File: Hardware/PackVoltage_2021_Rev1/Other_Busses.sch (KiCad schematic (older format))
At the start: 50 parts, among them Q10 Q_NMOS_DGS, Q6 Q_NMOS_DGS, Q7 Q_NMOS_DGS, Q8 Q_NMOS_DGS, Q9 Q_NMOS_DGS, U14 LT1910, U15 LT1910, U16 LT1910, U17 INA281, U18 INA281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

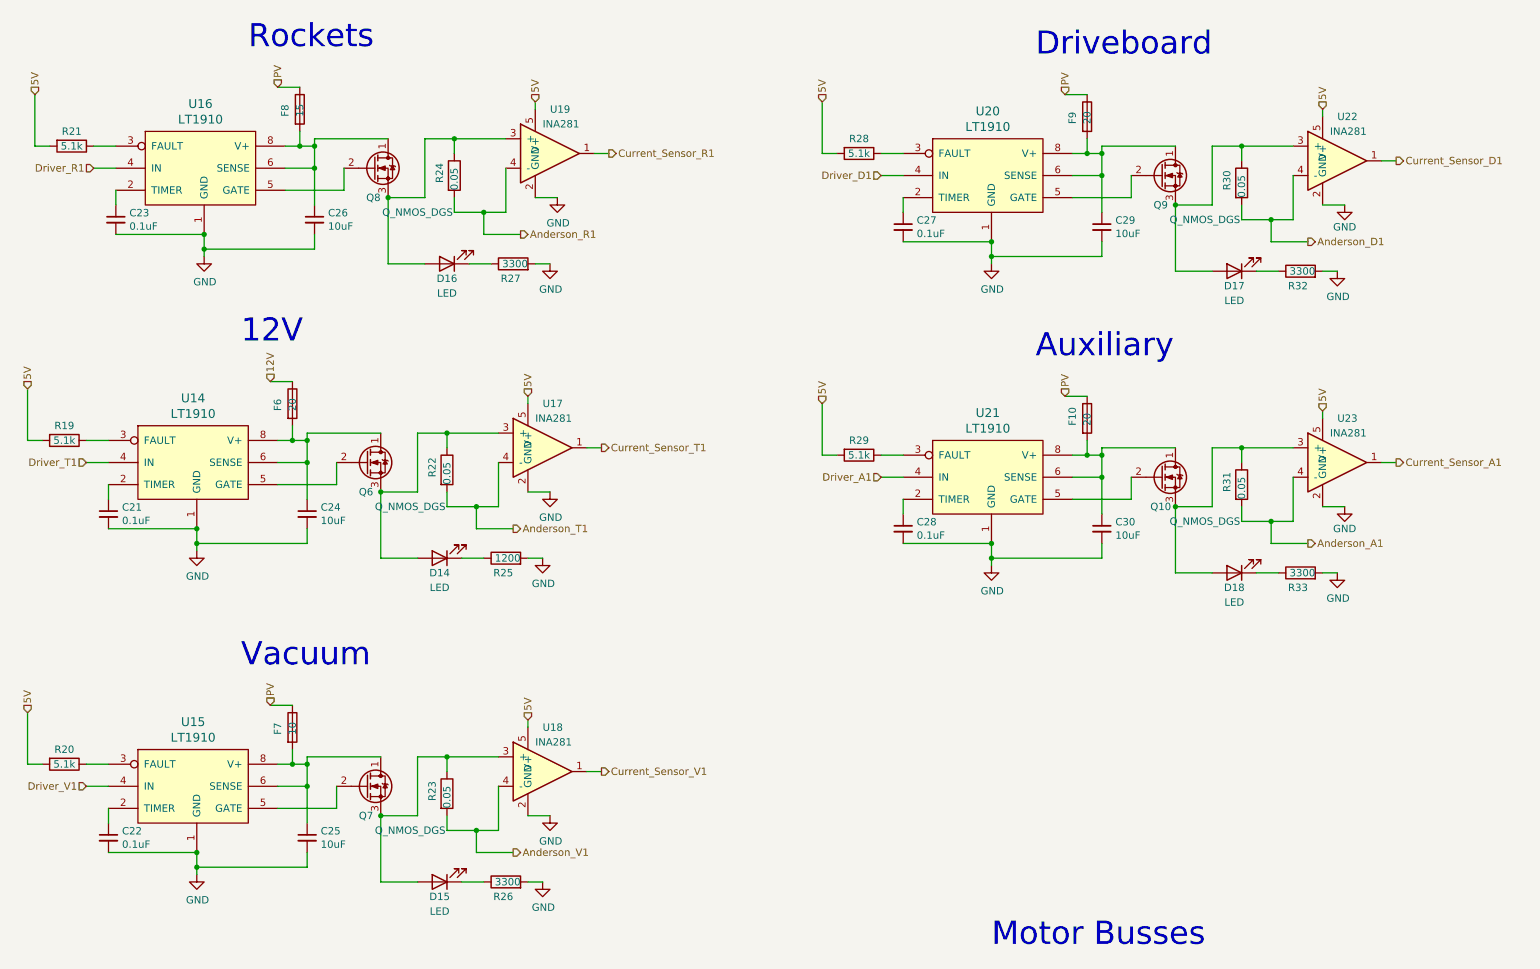
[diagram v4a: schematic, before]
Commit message: Finished Busses, Fixed Vias in Pads, Connected Okis & Buck
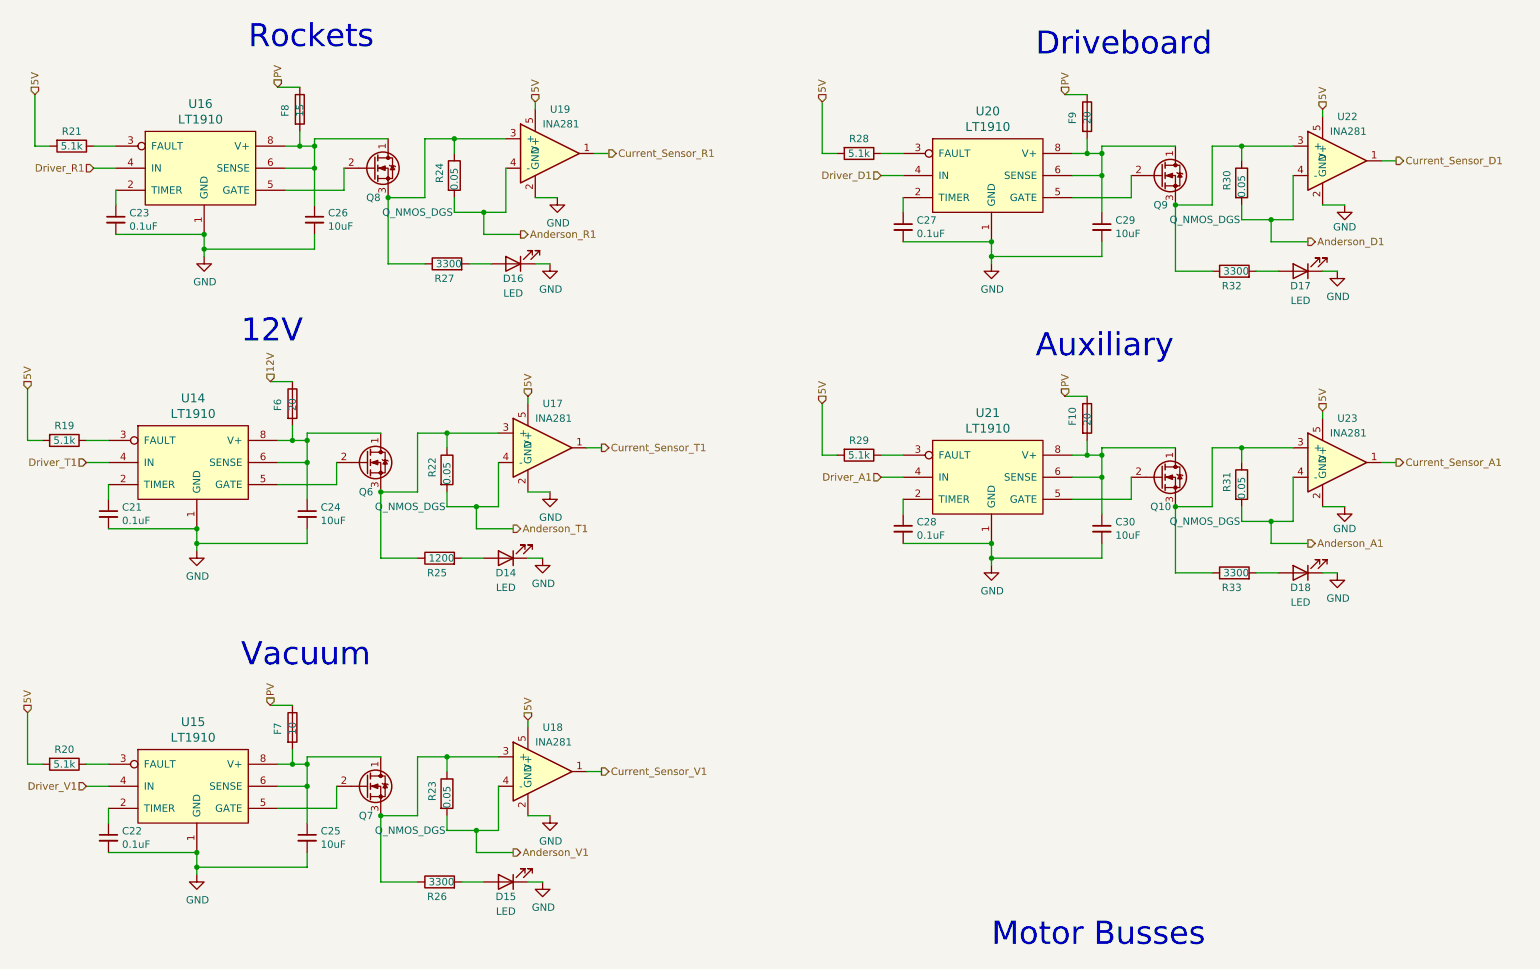
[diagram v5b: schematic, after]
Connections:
- net GND: now also D14.1 (K), D15.1 (K), D16.1 (K), D17.1 (K), D18.1 (K); no longer R25.2, R26.2, R27.2, R32.2, R33.2
- net at Q8.3 (S), R24.1, U19.3 (+): now also R27.1; no longer D16.2 (A)
- net at Q7.3 (S), R23.1, U18.3 (+): now also R26.1; no longer D15.2 (A)
- net at Q9.3 (S), R30.1, U22.3 (+): now also R32.1; no longer D17.2 (A)
- net at Q10.3 (S), R31.1, U23.3 (+): now also R33.1; no longer D18.2 (A)
- net at Q6.3 (S), R22.1, U17.3 (+): now also R25.1; no longer D14.2 (A)
- new net: D16.2 (A), R27.2
- new net: D15.2 (A), R26.2
- new net: D17.2 (A), R32.2
- new net: D18.2 (A), R33.2
- new net: D14.2 (A), R25.2
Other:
- moved on the sheet: D14, D15, D16, D17, D18, R25, R26, R27, R32, R33
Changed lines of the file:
@@
 L Device:LED D?
 U 1 1 5F846899
-P 3500 2300
+P 3950 2300
 AR Path="/5F7A6A8B/5F846899" Ref="D?"  Part="1"
 AR Path="/5F8EFCC9/5F846899" Ref="D16"  Part="1"
-F 0 "D16" H 3500 2400 50  0000 C CNN
-F 1 "LED" H 3500 2500 50  0000 C CNN
-F 2 "LED_SMD:LED_0603_1608Metric_Pad1.05x0.95mm_HandSolder" H 3500 2300 50  0001 C CNN
+F 0 "D16" H 3950 2400 50  0000 C CNN
+F 1 "LED" H 3950 2500 50  0000 C CNN
+F 2 "LED_SMD:LED_0603_1608Metric_Pad1.05x0.95mm_HandSolder" H 3950 2300 50  0001 C CNN
+F 3 "~" H 3950 2300 50  0001 C CNN
+	1    3950 2300
+	-1   0    0    1
+$EndComp
+Wire Wire Line
+	3100 2300 3350 2300
+$Comp
+L Device:R R?
+U 1 1 5F9AF792
+P 3500 2300
+AR Path="/5F7A6A8B/5F9AF792" Ref="R?"  Part="1"
+AR Path="/5F8EFCC9/5F9AF792" Ref="R27"  Part="1"
+F 0 "R27" V 3400 2250 50  0000 L CNN
+F 1 "3300" V 3500 2200 50  0000 L CNN
+F 2 "Resistor_SMD:R_0603_1608Metric_Pad1.05x0.95mm_HandSolder" V 3430 2300 50  0001 C CNN
 F 3 "~" H 3500 2300 50  0001 C CNN
 	1    3500 2300
-	-1   0    0    1
-$EndComp
-Wire Wire Line
-	3100 2300 3350 2300
-$Comp
-L Device:R R?
-U 1 1 5F9AF792
-P 3950 2300
-AR Path="/5F7A6A8B/5F9AF792" Ref="R?"  Part="1"
-AR Path="/5F8EFCC9/5F9AF792" Ref="R27"  Part="1"
-F 0 "R27" V 3850 2250 50  0000 L CNN
-F 1 "3300" V 3950 2200 50  0000 L CNN
-F 2 "Resistor_SMD:R_0603_1608Metric_Pad1.05x0.95mm_HandSolder" V 3880 2300 50  0001 C CNN
-F 3 "~" H 3950 2300 50  0001 C CNN
-	1    3950 2300
 	0    -1   -1   0
 $EndComp
@@
 	1    0    0    -1
 $EndComp
-$Comp
-L Device:LED D?
-U 1 1 5F9AF79C
-P 3450 4300
-AR Path="/5F7A6A8B/5F9AF79C" Ref="D?"  Part="1"
-AR Path="/5F8EFCC9/5F9AF79C" Ref="D14"  Part="1"
-F 0 "D14" H 3450 4400 50  0000 C CNN
-F 1 "LED" H 3450 4500 50  0000 C CNN
-F 2 "LED_SMD:LED_0603_1608Metric_Pad1.05x0.95mm_HandSolder" H 3450 4300 50  0001 C CNN
-F 3 "~" H 3450 4300 50  0001 C CNN
-	1    3450 4300
-	-1   0    0    1
-$EndComp
 Wire Wire Line
 	3050 4300 3300 4300
@@
 L Device:LED D?
 U 1 1 5F8A5A26
-P 3450 6500
+P 3900 6500
 AR Path="/5F7A6A8B/5F8A5A26" Ref="D?"  Part="1"
 AR Path="/5F8EFCC9/5F8A5A26" Ref="D15"  Part="1"
-F 0 "D15" H 3450 6600 50  0000 C CNN
-F 1 "LED" H 3450 6700 50  0000 C CNN
-F 2 "LED_SMD:LED_0603_1608Metric_Pad1.05x0.95mm_HandSolder" H 3450 6500 50  0001 C CNN
-F 3 "~" H 3450 6500 50  0001 C CNN
-	1    3450 6500
+F 0 "D15" H 3900 6600 50  0000 C CNN
+F 1 "LED" H 3900 6700 50  0000 C CNN
+F 2 "LED_SMD:LED_0603_1608Metric_Pad1.05x0.95mm_HandSolder" H 3900 6500 50  0001 C CNN
+F 3 "~" H 3900 6500 50  0001 C CNN
+	1    3900 6500
 	-1   0    0    1
 $EndComp
@@
 L Device:LED D?
 U 1 1 5F8B2B79
-P 8850 2350
+P 9300 2350
 AR Path="/5F7A6A8B/5F8B2B79" Ref="D?"  Part="1"
 AR Path="/5F8EFCC9/5F8B2B79" Ref="D17"  Part="1"
-F 0 "D17" H 8850 2450 50  0000 C CNN
-F 1 "LED" H 8850 2550 50  0000 C CNN
-F 2 "LED_SMD:LED_0603_1608Metric_Pad1.05x0.95mm_HandSolder" H 8850 2350 50  0001 C CNN
+F 0 "D17" H 9300 2450 50  0000 C CNN
+F 1 "LED" H 9300 2550 50  0000 C CNN
+F 2 "LED_SMD:LED_0603_1608Metric_Pad1.05x0.95mm_HandSolder" H 9300 2350 50  0001 C CNN
+F 3 "~" H 9300 2350 50  0001 C CNN
+	1    9300 2350
+	-1   0    0    1
+$EndComp
+Wire Wire Line
+	8450 2350 8700 2350
+$Comp
+L Device:R R?
+U 1 1 5F9AF7B7
+P 8850 2350
+AR Path="/5F7A6A8B/5F9AF7B7" Ref="R?"  Part="1"
+AR Path="/5F8EFCC9/5F9AF7B7" Ref="R32"  Part="1"
+F 0 "R32" V 8750 2300 50  0000 L CNN
+F 1 "3300" V 8850 2250 50  0000 L CNN
+F 2 "Resistor_SMD:R_0603_1608Metric_Pad1.05x0.95mm_HandSolder" V 8780 2350 50  0001 C CNN
 F 3 "~" H 8850 2350 50  0001 C CNN
 	1    8850 2350
-	-1   0    0    1
-$EndComp
-Wire Wire Line
-	8450 2350 8700 2350
-$Comp
-L Device:R R?
-U 1 1 5F9AF7B7
-P 9300 2350
-AR Path="/5F7A6A8B/5F9AF7B7" Ref="R?"  Part="1"
-AR Path="/5F8EFCC9/5F9AF7B7" Ref="R32"  Part="1"
-F 0 "R32" V 9200 2300 50  0000 L CNN
-F 1 "3300" V 9300 2250 50  0000 L CNN
-F 2 "Resistor_SMD:R_0603_1608Metric_Pad1.05x0.95mm_HandSolder" V 9230 2350 50  0001 C CNN
-F 3 "~" H 9300 2350 50  0001 C CNN
-	1    9300 2350
 	0    -1   -1   0
 $EndComp
@@
 L Device:LED D?
 U 1 1 5F8E4236
-P 8850 4400
+P 9300 4400
 AR Path="/5F7A6A8B/5F8E4236" Ref="D?"  Part="1"
 AR Path="/5F8EFCC9/5F8E4236" Ref="D18"  Part="1"
-F 0 "D18" H 8850 4500 50  0000 C CNN
-F 1 "LED" H 8850 4600 50  0000 C CNN
-F 2 "LED_SMD:LED_0603_1608Metric_Pad1.05x0.95mm_HandSolder" H 8850 4400 50  0001 C CNN
+F 0 "D18" H 9300 4500 50  0000 C CNN
+F 1 "LED" H 9300 4600 50  0000 C CNN
+F 2 "LED_SMD:LED_0603_1608Metric_Pad1.05x0.95mm_HandSolder" H 9300 4400 50  0001 C CNN
+F 3 "~" H 9300 4400 50  0001 C CNN
+	1    9300 4400
+	-1   0    0    1
+$EndComp
+Wire Wire Line
+	8450 4400 8700 4400
+$Comp
+L Device:R R?
+U 1 1 5F8E423D
+P 8850 4400
+AR Path="/5F7A6A8B/5F8E423D" Ref="R?"  Part="1"
+AR Path="/5F8EFCC9/5F8E423D" Ref="R33"  Part="1"
+F 0 "R33" V 8750 4350 50  0000 L CNN
+F 1 "3300" V 8850 4300 50  0000 L CNN
+F 2 "Resistor_SMD:R_0603_1608Metric_Pad1.05x0.95mm_HandSolder" V 8780 4400 50  0001 C CNN
 F 3 "~" H 8850 4400 50  0001 C CNN
 	1    8850 4400
-	-1   0    0    1
-$EndComp
-Wire Wire Line
-	8450 4400 8700 4400
-$Comp
-L Device:R R?
-U 1 1 5F8E423D
-P 9300 4400
-AR Path="/5F7A6A8B/5F8E423D" Ref="R?"  Part="1"
-AR Path="/5F8EFCC9/5F8E423D" Ref="R33"  Part="1"
-F 0 "R33" V 9200 4350 50  0000 L CNN
-F 1 "3300" V 9300 4300 50  0000 L CNN
-F 2 "Resistor_SMD:R_0603_1608Metric_Pad1.05x0.95mm_HandSolder" V 9230 4400 50  0001 C CNN
-F 3 "~" H 9300 4400 50  0001 C CNN
-	1    9300 4400
 	0    -1   -1   0
 $EndComp
@@
 $Comp
 L Device:R R?
+U 1 1 5F9AF79D
+P 3450 4300
+AR Path="/5F7A6A8B/5F9AF79D" Ref="R?"  Part="1"
+AR Path="/5F8EFCC9/5F9AF79D" Ref="R25"  Part="1"
+F 0 "R25" V 3350 4250 50  0000 L CNN
+F 1 "1200" V 3450 4200 50  0000 L CNN
+F 2 "Resistor_SMD:R_0603_1608Metric_Pad1.05x0.95mm_HandSolder" V 3380 4300 50  0001 C CNN
+F 3 "~" H 3450 4300 50  0001 C CNN
+	1    3450 4300
+	0    -1   -1   0
+$EndComp
+$Comp
+L Device:LED D?
+U 1 1 5F9AF79C
+P 3900 4300
+AR Path="/5F7A6A8B/5F9AF79C" Ref="D?"  Part="1"
+AR Path="/5F8EFCC9/5F9AF79C" Ref="D14"  Part="1"
+F 0 "D14" H 3900 4400 50  0000 C CNN
+F 1 "LED" H 3900 4500 50  0000 C CNN
+F 2 "LED_SMD:LED_0603_1608Metric_Pad1.05x0.95mm_HandSolder" H 3900 4300 50  0001 C CNN
+F 3 "~" H 3900 4300 50  0001 C CNN
+	1    3900 4300
+	-1   0    0    1
+$EndComp
+$Comp
+L Device:R R?
 U 1 1 5F9AF7AA
-P 3900 6500
+P 3450 6500
 AR Path="/5F7A6A8B/5F9AF7AA" Ref="R?"  Part="1"
 AR Path="/5F8EFCC9/5F9AF7AA" Ref="R26"  Part="1"
-F 0 "R26" V 3800 6450 50  0000 L CNN
-F 1 "3300" V 3900 6400 50  0000 L CNN
-F 2 "Resistor_SMD:R_0603_1608Metric_Pad1.05x0.95mm_HandSolder" V 3830 6500 50  0001 C CNN
-F 3 "~" H 3900 6500 50  0001 C CNN
-	1    3900 6500
+F 0 "R26" V 3350 6450 50  0000 L CNN
+F 1 "3300" V 3450 6400 50  0000 L CNN
+F 2 "Resistor_SMD:R_0603_1608Metric_Pad1.05x0.95mm_HandSolder" V 3380 6500 50  0001 C CNN
+F 3 "~" H 3450 6500 50  0001 C CNN
+	1    3450 6500
 	0    -1   -1   0
 $EndComp
-$Comp
-L Device:R R?
-U 1 1 5F9AF79D
-P 3900 4300
-AR Path="/5F7A6A8B/5F9AF79D" Ref="R?"  Part="1"
-AR Path="/5F8EFCC9/5F9AF79D" Ref="R25"  Part="1"
-F 0 "R25" V 3800 4250 50  0000 L CNN
-F 1 "1200" V 3900 4200 50  0000 L CNN
-F 2 "Resistor_SMD:R_0603_1608Metric_Pad1.05x0.95mm_HandSolder" V 3830 4300 50  0001 C CNN
-F 3 "~" H 3900 4300 50  0001 C CNN
-	1    3900 4300
-	0    -1   -1   0
-$EndComp

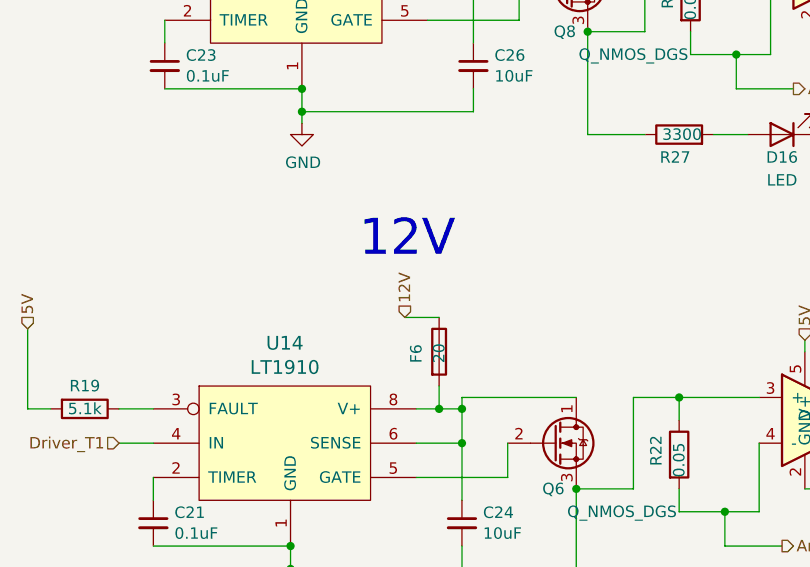
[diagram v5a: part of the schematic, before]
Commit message: Edge Cuts
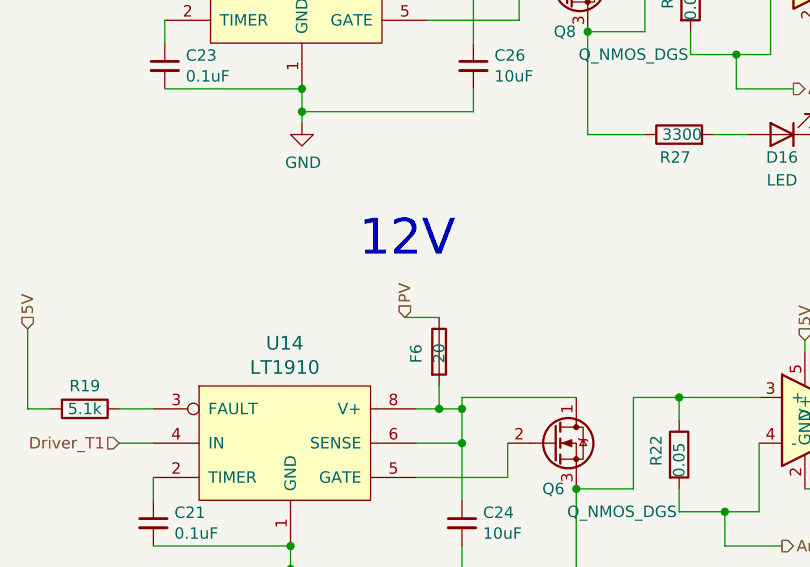
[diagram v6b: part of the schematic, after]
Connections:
- net 12V is gone; now on net PV: F6.1
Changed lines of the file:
@@
 $Descr A4 11693 8268
 encoding utf-8
-Sheet 4 5
+Sheet 3 5
 Title ""
 Date ""
@@
 	4050 4300 4150 4300
 Text HLabel 2300 3100 1    50   Input ~ 0
-12V
+PV
 $Comp
 L PackVoltage_2021_Rev1-rescue:INA281-MRDT_ICs U?

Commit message: footprint update
-andersons made vertical
-current resistor footprint updated
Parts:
- R22, R23, R24, R30, R31: footprint Package_TO_SOT_SMD:TO-263-2_TabPin1 -> Resistor_SMD:R_2512_6332Metric_Pad1.40x3.35mm_HandSolder
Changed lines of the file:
@@
 F 0 "R24" V 3450 1650 50  0000 L CNN
 F 1 "0.05" V 3550 1600 50  0000 L CNN
-F 2 "Package_TO_SOT_SMD:TO-263-2_TabPin1" V 3480 1700 50  0001 C CNN
+F 2 "Resistor_SMD:R_2512_6332Metric_Pad1.40x3.35mm_HandSolder" V 3480 1700 50  0001 C CNN
 F 3 "https://riedon.com/media/pdf/PFS35.pdf" H 3550 1700 50  0001 C CNN
 	1    3550 1700
@@
 F 0 "R22" V 3400 3650 50  0000 L CNN
 F 1 "0.05" V 3500 3600 50  0000 L CNN
-F 2 "Package_TO_SOT_SMD:TO-263-2_TabPin1" V 3430 3700 50  0001 C CNN
+F 2 "Resistor_SMD:R_2512_6332Metric_Pad1.40x3.35mm_HandSolder" V 3430 3700 50  0001 C CNN
 F 3 "https://riedon.com/media/pdf/PFS35.pdf" H 3500 3700 50  0001 C CNN
 	1    3500 3700
@@
 F 0 "R23" V 3400 5850 50  0000 L CNN
 F 1 "0.05" V 3500 5800 50  0000 L CNN
-F 2 "Package_TO_SOT_SMD:TO-263-2_TabPin1" V 3430 5900 50  0001 C CNN
+F 2 "Resistor_SMD:R_2512_6332Metric_Pad1.40x3.35mm_HandSolder" V 3430 5900 50  0001 C CNN
 F 3 "https://riedon.com/media/pdf/PFS35.pdf" H 3500 5900 50  0001 C CNN
 	1    3500 5900
@@
 F 0 "R30" V 8800 1700 50  0000 L CNN
 F 1 "0.05" V 8900 1650 50  0000 L CNN
-F 2 "Package_TO_SOT_SMD:TO-263-2_TabPin1" V 8830 1750 50  0001 C CNN
+F 2 "Resistor_SMD:R_2512_6332Metric_Pad1.40x3.35mm_HandSolder" V 8830 1750 50  0001 C CNN
 F 3 "https://riedon.com/media/pdf/PFS35.pdf" H 8900 1750 50  0001 C CNN
 	1    8900 1750
@@
 F 0 "R31" V 8800 3750 50  0000 L CNN
 F 1 "0.05" V 8900 3700 50  0000 L CNN
-F 2 "Package_TO_SOT_SMD:TO-263-2_TabPin1" V 8830 3800 50  0001 C CNN
+F 2 "Resistor_SMD:R_2512_6332Metric_Pad1.40x3.35mm_HandSolder" V 8830 3800 50  0001 C CNN
 F 3 "https://riedon.com/media/pdf/PFS35.pdf" H 8900 3800 50  0001 C CNN
 	1    8900 3800
